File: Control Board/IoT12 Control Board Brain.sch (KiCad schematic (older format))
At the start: 36 parts, among them J10 USB_B_Micro, J11 Conn_ARM_JTAG_SWD_10, J9 Conn_ARM_JTAG_SWD_10, SW2 SW_Push, U1 ATSAMD21G18A-AU, U6 AT24C32, Y1 32768Hz

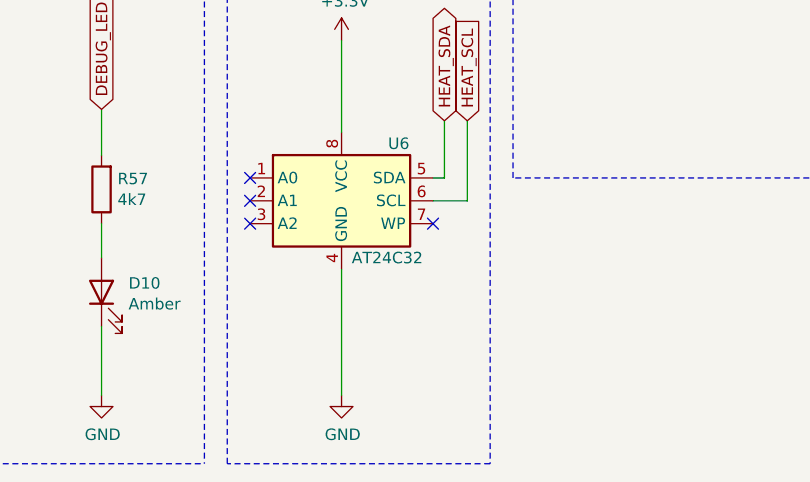
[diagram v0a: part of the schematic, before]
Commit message: Added I2C addresses to silkscreen and schematic.
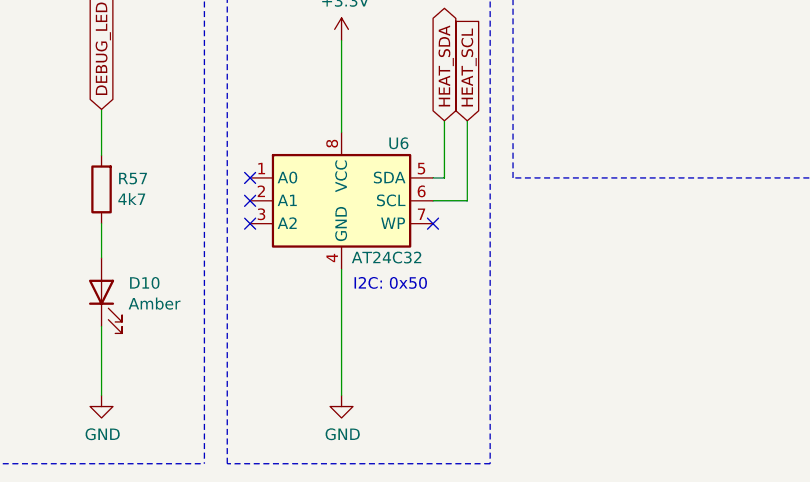
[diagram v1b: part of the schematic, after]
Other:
- note added: "I2C: 0x50"
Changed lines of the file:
@@
 Wire Wire Line
 	5100 4800 5200 4800
+Text Notes 6250 6950 0    50   ~ 0
+I2C: 0x50
 $EndSCHEMATC

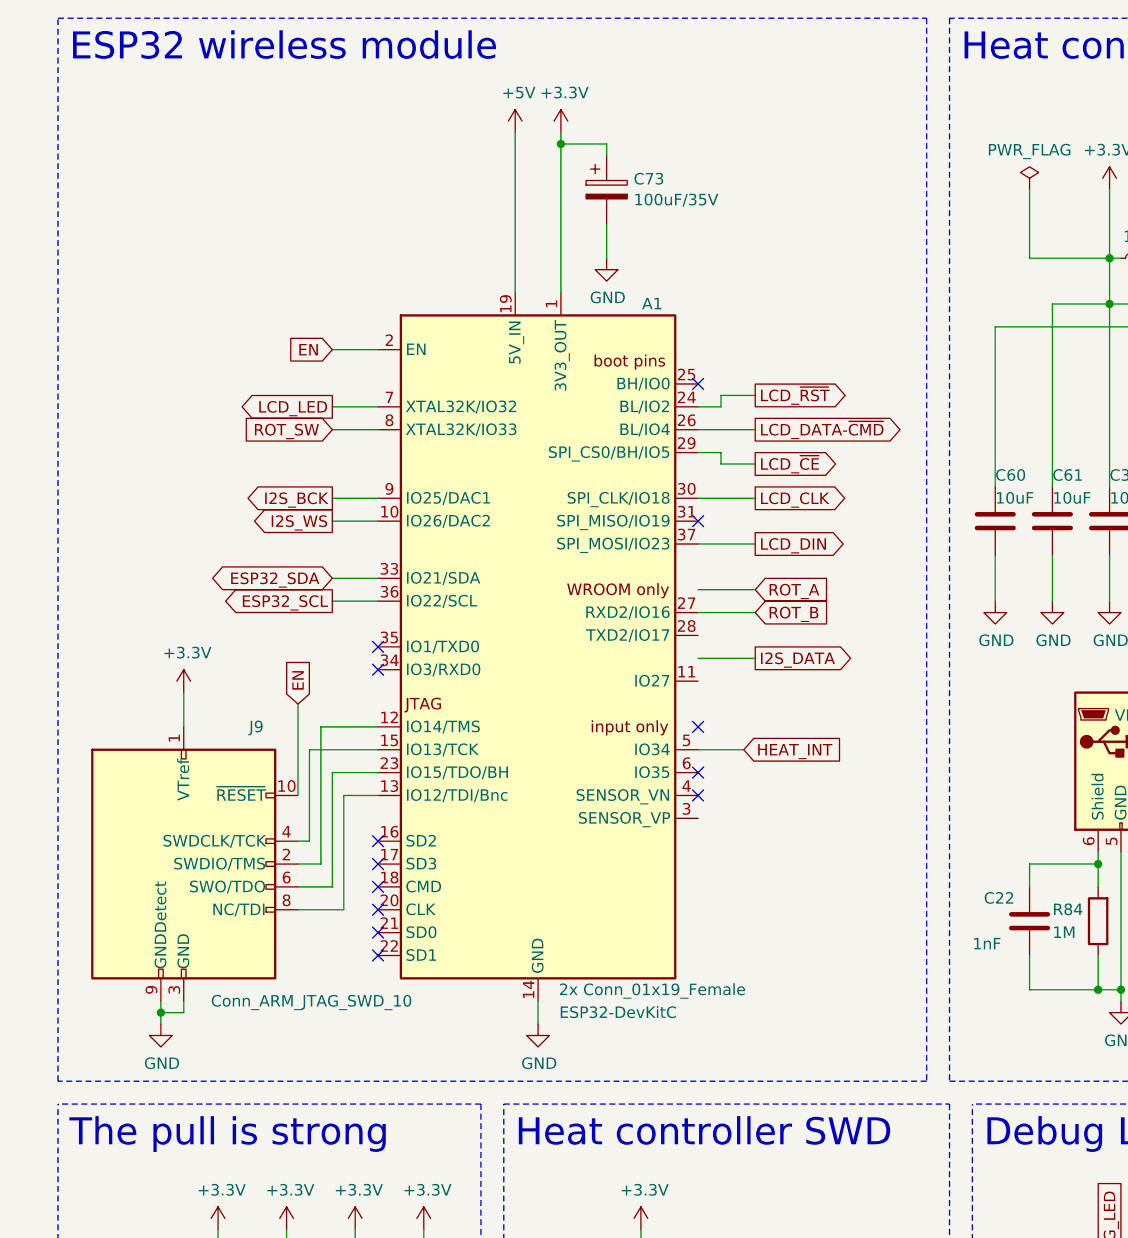
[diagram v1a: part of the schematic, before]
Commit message: More testing and re-added voltage monitor.
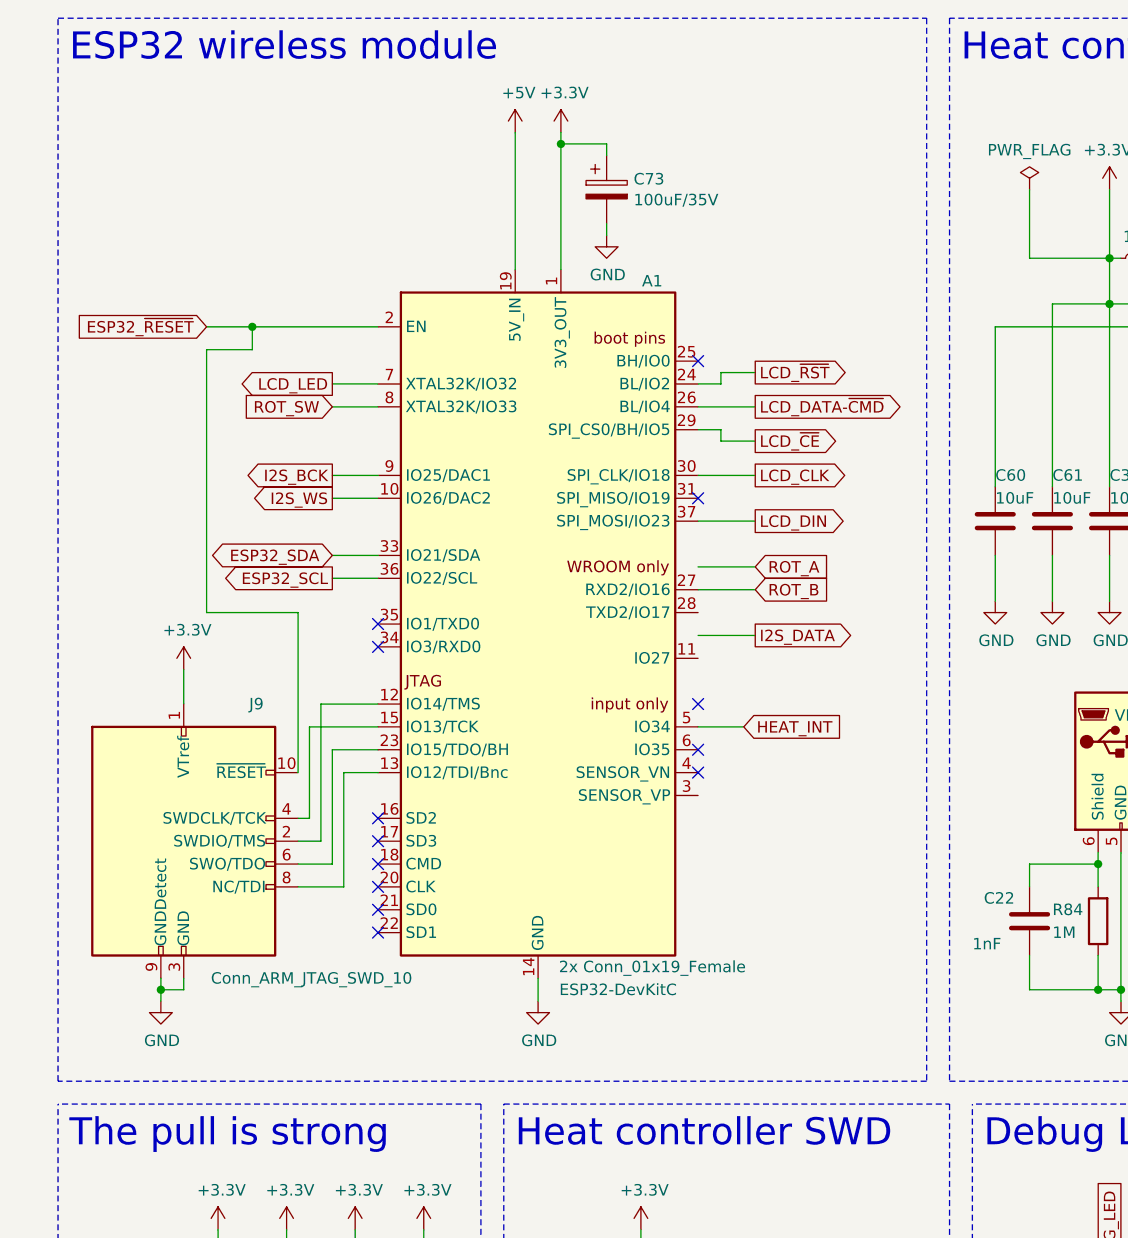
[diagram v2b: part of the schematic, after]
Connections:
- net EN renamed ESP32_~RESET
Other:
- moved on the sheet: A1, J9
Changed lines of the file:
@@
 L power:GND #PWR0153
 U 1 1 5FF0E00E
-P 2650 4950
-F 0 "#PWR0153" H 2650 4700 50  0001 C CNN
-F 1 "GND" H 2655 4777 50  0000 C CNN
-F 2 "" H 2650 4950 50  0001 C CNN
-F 3 "" H 2650 4950 50  0001 C CNN
-	1    2650 4950
+P 2650 4850
+F 0 "#PWR0153" H 2650 4600 50  0001 C CNN
+F 1 "GND" H 2655 4677 50  0000 C CNN
+F 2 "" H 2650 4850 50  0001 C CNN
+F 3 "" H 2650 4850 50  0001 C CNN
+	1    2650 4850
 	1    0    0    -1
 $EndComp
@@
 Text Notes 600  750  0    118  ~ 0
 ESP32 wireless module
-Text GLabel 1750 2250 0    50   Output ~ 0
+Text GLabel 1750 2150 0    50   Output ~ 0
 LCD_LED
 Wire Wire Line
-	1750 2250 1950 2250
-Text GLabel 1750 3000 0    50   BiDi ~ 0
+	1750 2150 1950 2150
+Text GLabel 1750 2900 0    50   BiDi ~ 0
 ESP32_SDA
-Text GLabel 1750 3100 0    50   Output ~ 0
+Text GLabel 1750 3000 0    50   Output ~ 0
 ESP32_SCL
 Wire Wire Line
 	2750 1050 2750 1100
+NoConn ~ 1950 4050
 NoConn ~ 1950 4150
 NoConn ~ 1950 4250
@@
 NoConn ~ 1950 4450
 NoConn ~ 1950 4550
-NoConn ~ 1950 4650
-Text GLabel 3600 2500 2    50   Output ~ 0
+Text GLabel 3600 2400 2    50   Output ~ 0
 LCD_~CE
-Text GLabel 3600 2650 2    50   Output ~ 0
+Text GLabel 3600 2550 2    50   Output ~ 0
 LCD_CLK
-Text GLabel 3600 2850 2    50   Output ~ 0
+Text GLabel 3600 2750 2    50   Output ~ 0
 LCD_DIN
-Text GLabel 3600 2200 2    50   Output ~ 0
+Text GLabel 3600 2100 2    50   Output ~ 0
 LCD_~RST
-Text GLabel 3600 2350 2    50   Output ~ 0
+Text GLabel 3600 2250 2    50   Output ~ 0
 LCD_DATA-~CMD
-Text GLabel 1750 2350 0    50   Input ~ 0
+Text GLabel 1750 2250 0    50   Input ~ 0
 ROT_SW
+Text GLabel 3600 2950 2    50   Input ~ 0
+ROT_A
+Wire Wire Line
+	3350 2950 3600 2950
 Text GLabel 3600 3050 2    50   Input ~ 0
-ROT_A
-Wire Wire Line
-	3350 3050 3600 3050
-Text GLabel 3600 3150 2    50   Input ~ 0
 ROT_B
 Wire Wire Line
-	3600 3150 3350 3150
+	3600 3050 3350 3050
 $Comp
 L MCU_Module-extra:ESP32-DevKitC A1
 U 1 1 5FF09372
-P 2650 3050
-F 0 "A1" H 3150 4300 50  0000 C CNN
-F 1 "2x Conn_01x19_Female" H 3150 1300 50  0000 C CNN
-F 2 "Module-extra:ESP32-DevKitC" H 2650 1150 50  0001 C CNN
-F 3 "https://www.espressif.com/sites/default/files/documentation/esp32-wroom-32_datasheet_en.pdf" H 2350 2950 50  0001 C CNN
-F 4 "ESP32-DevKitC" H 3000 1200 50  0000 C CNN "Description"
-	1    2650 3050
-	1    0    0    -1
-$EndComp
-NoConn ~ 3350 2750
-Wire Wire Line
-	3450 2250 3450 2200
-Wire Wire Line
-	3450 2200 3600 2200
-Wire Wire Line
-	3350 2250 3450 2250
-Wire Wire Line
-	3350 2350 3600 2350
-Wire Wire Line
-	3350 2450 3450 2450
-Wire Wire Line
-	3450 2450 3450 2500
-Wire Wire Line
-	3450 2500 3600 2500
-Wire Wire Line
-	3350 2650 3600 2650
-Wire Wire Line
-	3350 2850 3600 2850
-Wire Wire Line
-	1750 2350 1950 2350
-Wire Wire Line
-	2650 4850 2650 4950
-Wire Wire Line
-	3350 3750 3550 3750
+P 2650 2950
+F 0 "A1" H 3150 4200 50  0000 C CNN
+F 1 "2x Conn_01x19_Female" H 3150 1200 50  0000 C CNN
+F 2 "Module-extra:ESP32-DevKitC" H 2650 1050 50  0001 C CNN
+F 3 "https://www.espressif.com/sites/default/files/documentation/esp32-wroom-32_datasheet_en.pdf" H 2350 2850 50  0001 C CNN
+F 4 "ESP32-DevKitC" H 3000 1100 50  0000 C CNN "Description"
+	1    2650 2950
+	1    0    0    -1
+$EndComp
+NoConn ~ 3350 2650
+Wire Wire Line
+	3450 2150 3450 2100
+Wire Wire Line
+	3450 2100 3600 2100
+Wire Wire Line
+	3350 2150 3450 2150
+Wire Wire Line
+	3350 2250 3600 2250
+Wire Wire Line
+	3350 2350 3450 2350
+Wire Wire Line
+	3450 2350 3450 2400
+Wire Wire Line
+	3450 2400 3600 2400
+Wire Wire Line
+	3350 2550 3600 2550
+Wire Wire Line
+	3350 2750 3600 2750
+Wire Wire Line
+	1750 2250 1950 2250
+Wire Wire Line
+	2650 4750 2650 4850
+Wire Wire Line
+	3350 3650 3550 3650
 $Comp
 L MCU_Microchip_SAMD-extra:SAMD21G_ARDUINO_M0 U1
@@
 Wire Wire Line
 	5150 7100 5150 7400
+Text GLabel 1750 2550 0    50   Output ~ 0
+I2S_BCK
 Text GLabel 1750 2650 0    50   Output ~ 0
-I2S_BCK
-Text GLabel 1750 2750 0    50   Output ~ 0
 I2S_WS
 Wire Wire Line
-	1750 2650 1950 2650
-Wire Wire Line
-	1950 2750 1750 2750
-Text GLabel 3600 3350 2    50   Output ~ 0
+	1750 2550 1950 2550
+Wire Wire Line
+	1950 2650 1750 2650
+Text GLabel 3600 3250 2    50   Output ~ 0
 I2S_DATA
 Wire Wire Line
-	3350 3350 3600 3350
+	3350 3250 3600 3250
 Text GLabel 10500 3500 2    50   Input ~ 0
 NTC
@@
 L power:GND #PWR0137
 U 1 1 608EAD5C
-P 2950 1600
-F 0 "#PWR0137" H 2950 1350 50  0001 C CNN
-F 1 "GND" H 2955 1427 50  0000 C CNN
-F 2 "" H 2950 1600 50  0001 C CNN
-F 3 "" H 2950 1600 50  0001 C CNN
-	1    2950 1600
+P 2950 1500
+F 0 "#PWR0137" H 2950 1250 50  0001 C CNN
+F 1 "GND" H 2955 1327 50  0000 C CNN
+F 2 "" H 2950 1500 50  0001 C CNN
+F 3 "" H 2950 1500 50  0001 C CNN
+	1    2950 1500
 	1    0    0    -1
 $EndComp
@@
 Connection ~ 2750 1100
 Wire Wire Line
-	2750 1100 2750 1750
-Wire Wire Line
-	2950 1600 2950 1450
+	2750 1100 2750 1650
+Wire Wire Line
+	2950 1500 2950 1450
 NoConn ~ 7050 2850
+NoConn ~ 3350 3750
 NoConn ~ 3350 3850
-NoConn ~ 3350 3950
 Wire Notes Line
 	2400 5300 2400 7700
@@
 ESP32_SCL
 Wire Wire Line
-	1750 3100 1950 3100
+	1750 3000 1950 3000
 Wire Wire Line
 	1100 7150 1850 7150
@@
 ESP32_SDA
 Wire Wire Line
-	1750 3000 1950 3000
+	1750 2900 1950 2900
 Wire Wire Line
 	1100 7250 2150 7250
 Wire Wire Line
 	2150 6500 2150 7250
-NoConn ~ 3350 3650
-Text GLabel 3550 3750 2    50   Input ~ 0
+NoConn ~ 3350 3550
+Text GLabel 3550 3650 2    50   Input ~ 0
 HEAT_INT
 $Comp
@@
 Wire Wire Line
 	6750 6550 6750 6200
-NoConn ~ 1950 3400
 NoConn ~ 1950 3300
+NoConn ~ 1950 3200
 NoConn ~ 10250 3000
-NoConn ~ 3350 2150
+NoConn ~ 3350 2050
 $Comp
 L Connector:TestPoint TP1
@@
 L Connector:Conn_ARM_JTAG_SWD_10 J9
 U 1 1 6045AF4E
-P 1100 4250
-F 0 "J9" H 1450 4850 50  0000 R CNN
-F 1 "Conn_ARM_JTAG_SWD_10" H 2100 3650 50  0000 R CNN
-F 2 "Connector_PinHeader_2.54mm:PinHeader_2x05_P2.54mm_Vertical" H 1100 4250 50  0001 C CNN
-F 3 "http://infocenter.arm.com/help/topic/com.arm.doc.ddi0314h/DDI0314H_coresight_components_trm.pdf" V 750 3000 50  0001 C CNN
-	1    1100 4250
+P 1100 4150
+F 0 "J9" H 1450 4750 50  0000 R CNN
+F 1 "Conn_ARM_JTAG_SWD_10" H 2100 3550 50  0000 R CNN
+F 2 "Connector_PinHeader_2.54mm:PinHeader_2x05_P2.54mm_Vertical" H 1100 4150 50  0001 C CNN
+F 3 "http://infocenter.arm.com/help/topic/com.arm.doc.ddi0314h/DDI0314H_coresight_components_trm.pdf" V 750 2900 50  0001 C CNN
+	1    1100 4150
 	1    0    0    -1
 $EndComp
@@
 L power:GND #PWR04
 U 1 1 6045D9E5
-P 1000 4950
-F 0 "#PWR04" H 1000 4700 50  0001 C CNN
-F 1 "GND" H 1005 4777 50  0000 C CNN
-F 2 "" H 1000 4950 50  0001 C CNN
-F 3 "" H 1000 4950 50  0001 C CNN
-	1    1000 4950
-	1    0    0    -1
-$EndComp
-Wire Wire Line
-	1000 4950 1000 4900
-Wire Wire Line
-	1100 4850 1100 4900
-Wire Wire Line
-	1100 4900 1000 4900
-Connection ~ 1000 4900
-Wire Wire Line
-	1000 4900 1000 4850
+P 1000 4850
+F 0 "#PWR04" H 1000 4600 50  0001 C CNN
+F 1 "GND" H 1005 4677 50  0000 C CNN
+F 2 "" H 1000 4850 50  0001 C CNN
+F 3 "" H 1000 4850 50  0001 C CNN
+	1    1000 4850
+	1    0    0    -1
+$EndComp
+Wire Wire Line
+	1000 4850 1000 4800
+Wire Wire Line
+	1100 4750 1100 4800
+Wire Wire Line
+	1100 4800 1000 4800
+Connection ~ 1000 4800
+Wire Wire Line
+	1000 4800 1000 4750
 $Comp
 L power:+3.3V #PWR03
 U 1 1 60474EA3
-P 1100 3500
-F 0 "#PWR03" H 1100 3350 50  0001 C CNN
-F 1 "+3.3V" H 1115 3673 50  0000 C CNN
-F 2 "" H 1100 3500 50  0001 C CNN
-F 3 "" H 1100 3500 50  0001 C CNN
-	1    1100 3500
-	1    0    0    -1
-$EndComp
-Wire Wire Line
-	1100 3500 1100 3650
-Text GLabel 1750 2000 0    50   Input ~ 0
-EN
-Wire Wire Line
-	1750 2000 1950 2000
-Text GLabel 1600 3550 1    50   Input ~ 0
-EN
-Wire Wire Line
-	1600 3950 1600 3550
-Wire Wire Line
-	1950 3650 1700 3650
-Wire Wire Line
-	1700 3650 1700 4250
-Wire Wire Line
-	1700 4250 1600 4250
-Wire Wire Line
-	1950 3750 1650 3750
-Wire Wire Line
-	1650 3750 1650 4150
-Wire Wire Line
-	1650 4150 1600 4150
-Wire Wire Line
-	1950 3850 1750 3850
-Wire Wire Line
-	1750 3850 1750 4350
-Wire Wire Line
-	1750 4350 1600 4350
-Wire Wire Line
-	1600 4450 1800 4450
-Wire Wire Line
-	1800 4450 1800 3950
-Wire Wire Line
-	1800 3950 1950 3950
-Wire Wire Line
-	2550 1050 2550 1750
+P 1100 3400
+F 0 "#PWR03" H 1100 3250 50  0001 C CNN
+F 1 "+3.3V" H 1115 3573 50  0000 C CNN
+F 2 "" H 1100 3400 50  0001 C CNN
+F 3 "" H 1100 3400 50  0001 C CNN
+	1    1100 3400
+	1    0    0    -1
+$EndComp
+Wire Wire Line
+	1100 3400 1100 3550
+Text GLabel 1200 1900 0    50   Input ~ 0
+ESP32_~RESET
+Wire Wire Line
+	1200 1900 1400 1900
+Wire Wire Line
+	1950 3550 1700 3550
+Wire Wire Line
+	1700 3550 1700 4150
+Wire Wire Line
+	1700 4150 1600 4150
+Wire Wire Line
+	1950 3650 1650 3650
+Wire Wire Line
+	1650 3650 1650 4050
+Wire Wire Line
+	1650 4050 1600 4050
+Wire Wire Line
+	1950 3750 1750 3750
+Wire Wire Line
+	1750 3750 1750 4250
+Wire Wire Line
+	1750 4250 1600 4250
+Wire Wire Line
+	1600 4350 1800 4350
+Wire Wire Line
+	1800 4350 1800 3850
+Wire Wire Line
+	1800 3850 1950 3850
+Wire Wire Line
+	2550 1050 2550 1650
 Text Label 10250 1600 0    50   ~ 0
 D0
@@
 Text Notes 6250 6950 0    50   ~ 0
 I2C: 0x50
+Wire Wire Line
+	1600 3150 1200 3150
+Wire Wire Line
+	1200 3150 1200 2000
+Wire Wire Line
+	1200 2000 1400 2000
+Wire Wire Line
+	1400 2000 1400 1900
+Wire Wire Line
+	1600 3150 1600 3850
+Connection ~ 1400 1900
+Wire Wire Line
+	1400 1900 1950 1900
 $EndSCHEMATC

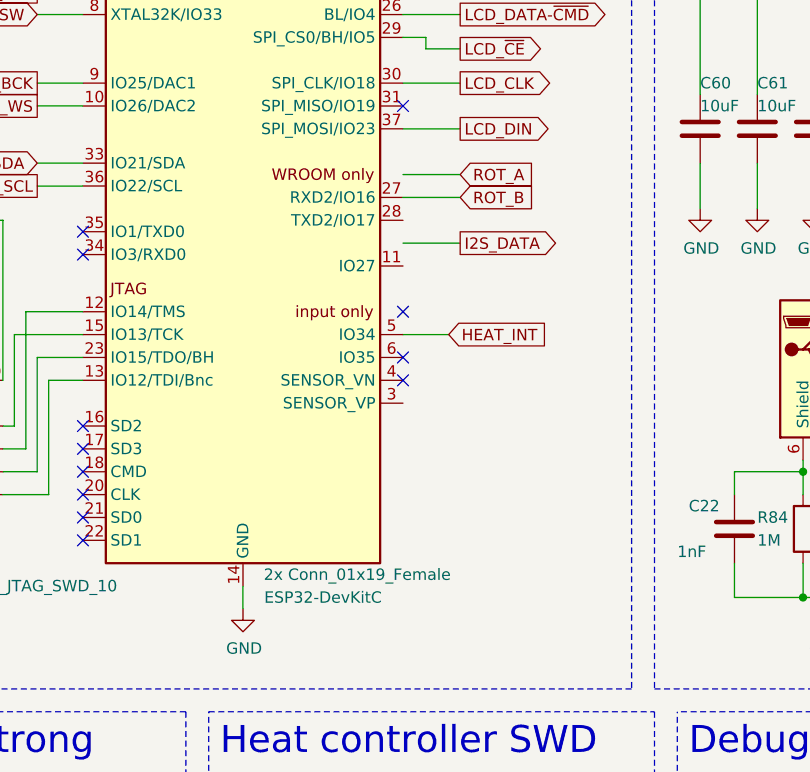
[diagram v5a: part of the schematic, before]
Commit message: Added ~RESET pulldown resistor.
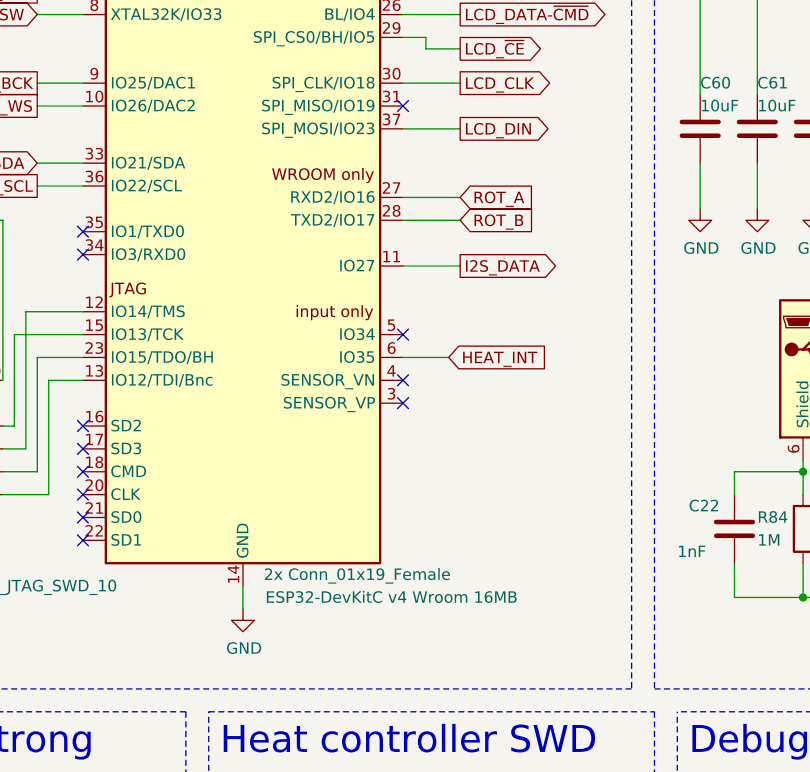
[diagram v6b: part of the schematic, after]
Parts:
- A1: Description ESP32-DevKitC -> ESP32-DevKitC v4 Wroom 16MB
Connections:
- net HEAT_INT: now also A1.6 (IO35); no longer A1.5 (IO34)
- net I2S_DATA: now also A1.11 (IO27)
- net ROT_A: now also A1.27 (RXD2/IO16)
- net ROT_B: now also A1.28 (TXD2/IO17); no longer A1.27 (RXD2/IO16)
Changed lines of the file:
@@
 Text GLabel 1750 2250 0    50   Input ~ 0
 ROT_SW
-Text GLabel 3600 2950 2    50   Input ~ 0
+Text GLabel 3600 3050 2    50   Input ~ 0
 ROT_A
 Wire Wire Line
-	3350 2950 3600 2950
-Text GLabel 3600 3050 2    50   Input ~ 0
+	3350 3050 3600 3050
+Text GLabel 3600 3150 2    50   Input ~ 0
 ROT_B
 Wire Wire Line
-	3600 3050 3350 3050
+	3600 3150 3350 3150
 $Comp
 L MCU_Module-extra:ESP32-DevKitC A1
@@
 F 2 "Module-extra:ESP32-DevKitC" H 2650 1050 50  0001 C CNN
 F 3 "https://www.espressif.com/sites/default/files/documentation/esp32-wroom-32_datasheet_en.pdf" H 2350 2850 50  0001 C CNN
-F 4 "ESP32-DevKitC" H 3000 1100 50  0000 C CNN "Description"
+F 4 "ESP32-DevKitC v4 Wroom 16MB" H 3300 1100 50  0000 C CNN "Description"
 	1    2650 2950
 	1    0    0    -1
@@
 	2650 4750 2650 4850
 Wire Wire Line
-	3350 3650 3550 3650
+	3350 3750 3550 3750
 $Comp
 L MCU_Microchip_SAMD-extra:SAMD21G_ARDUINO_M0 U1
@@
 Wire Wire Line
 	1950 2650 1750 2650
-Text GLabel 3600 3250 2    50   Output ~ 0
+Text GLabel 3600 3350 2    50   Output ~ 0
 I2S_DATA
 Wire Wire Line
-	3350 3250 3600 3250
+	3350 3350 3600 3350
 Text GLabel 10500 3500 2    50   Input ~ 0
 NTC
@@
 	2950 1500 2950 1450
 NoConn ~ 7050 2850
-NoConn ~ 3350 3750
+NoConn ~ 3350 3950
 NoConn ~ 3350 3850
 Wire Notes Line
@@
 Wire Wire Line
 	2150 6500 2150 7250
-NoConn ~ 3350 3550
-Text GLabel 3550 3650 2    50   Input ~ 0
+NoConn ~ 3350 3650
+Text GLabel 3550 3750 2    50   Input ~ 0
 HEAT_INT
 $Comp

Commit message: Changed some footprints to that have 3d models.
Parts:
- U6: footprint Package_SO:SO-8_3.9x4.9mm_P1.27mm -> Package_SO:SOIC-8_3.9x4.9mm_P1.27mm
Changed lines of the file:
@@
 Sheet 4 5
 Title "IoT12-hardware brain"
-Date "2021-04-02"
+Date "2021-04-27"
 Rev "V2.1"
 Comp ""
@@
 F 0 "U6" H 6450 6800 50  0000 C CNN
 F 1 "AT24C32" H 6400 6300 50  0000 C CNN
-F 2 "Package_SO:SO-8_3.9x4.9mm_P1.27mm" H 6200 6550 50  0001 C CNN
+F 2 "Package_SO:SOIC-8_3.9x4.9mm_P1.27mm" H 6200 6550 50  0001 C CNN
 F 3 "http://ww1.microchip.com/downloads/en/DeviceDoc/21072G.pdf" H 6200 6550 50  0001 C CNN
 	1    6200 6550

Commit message: Changed usb connector to one that has a 3d model.
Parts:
- J10: footprint Connector_USB:USB_Micro-B_Amphenol_10118194_Horizontal -> Connector_USB-fixed:USB_Micro-B_Amphenol_10118194_Horizontal
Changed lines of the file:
@@
 F 0 "J10" H 5350 4150 50  0000 C CNN
 F 1 "USB_B_Micro" H 5450 3450 50  0000 C CNN
-F 2 "Connector_USB:USB_Micro-B_Amphenol_10118194_Horizontal" H 5350 3750 50  0001 C CNN
+F 2 "Connector_USB-fixed:USB_Micro-B_Amphenol_10118194_Horizontal" H 5350 3750 50  0001 C CNN
 F 3 "~" H 5350 3750 50  0001 C CNN
 	1    5200 3800
